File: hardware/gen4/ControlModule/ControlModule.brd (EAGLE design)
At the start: 46.4 x 67 mm, 39 parts, among them IC1 XMEGA16A4A

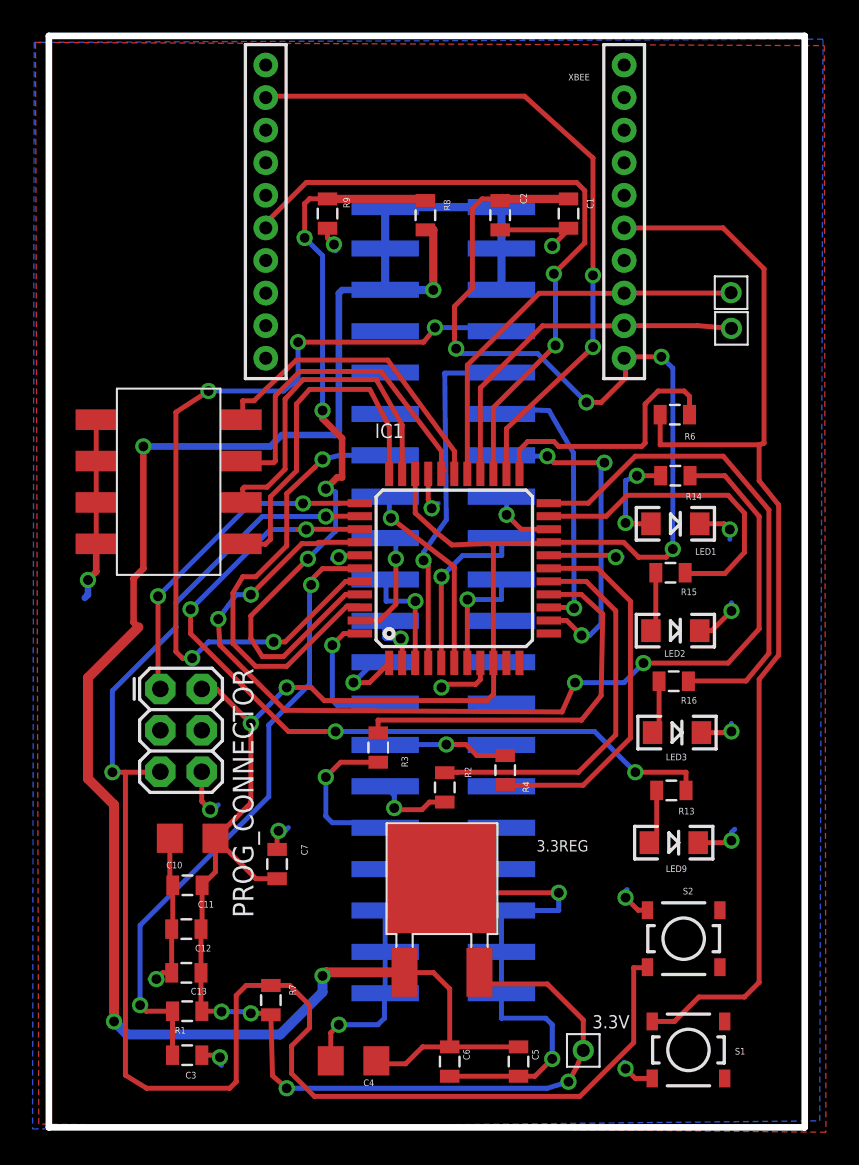
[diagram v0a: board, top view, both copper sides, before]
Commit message: fixed overlaps
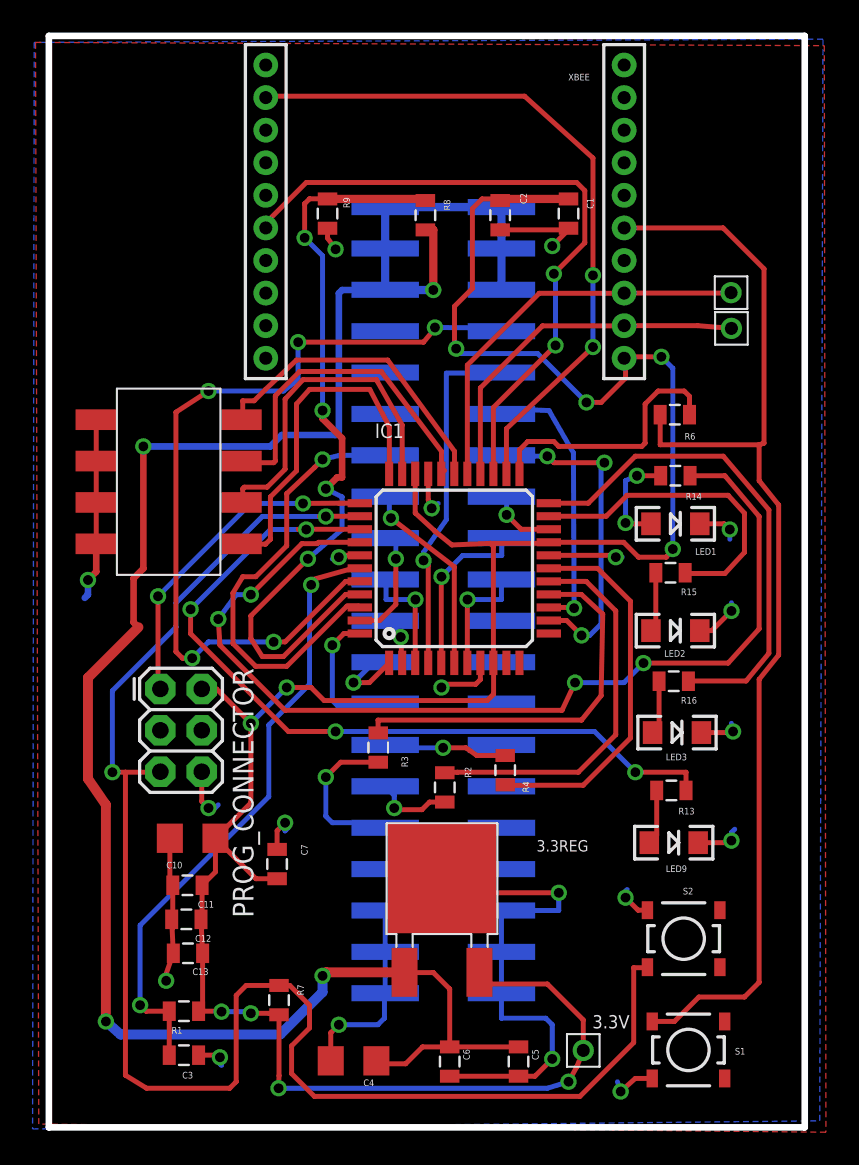
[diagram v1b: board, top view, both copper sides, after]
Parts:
- moved C13 1.20 mm to (32.7, 9.98)
- moved C12 0.60 mm to (32.6, 12.1)
- moved R7 0.50 mm to (38.3, 7.11)
- moved C3 0.20 mm to (32.5, 3.73)
- moved R1 0.20 mm to (32.5, 6.43)
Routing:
- net 3.3V: track 158.7 -> 160.7 mm
- net GND: track 63.8 -> 65.7 mm

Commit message: more gerber files. also all orders went through (technically)
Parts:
- removed PROG_CONNECTOR: FEMALE 2x3, SparkFun-Connectors:2X3
- added JP3: (no value), SparkFun-Connectors:2X5-SHROUDED
- moved C10 6.32 mm to (36.6, 11.8)
- moved C11 6.11 mm to (36.6, 9.46)
- moved R2 1.27 mm to (49.8, 20.2)
- moved C12 0.10 mm to (32.7, 12.1)
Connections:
- net 3.3V: now also JP3.2; no longer PROG_CONNECTOR.2
- net DATA: no longer PROG_CONNECTOR.1
- net GND: now also JP3.10, JP3.4, JP3.6, JP3.8; no longer PROG_CONNECTOR.6
- net MISO: now also JP3.9
- net MOSI: now also JP3.1
- net RESET: now also JP3.5; no longer PROG_CONNECTOR.5
- net SCK: now also JP3.7
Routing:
- net SCK: track 23.1 -> 53.1 mm, vias 0 -> 1
- net GND: track 65.7 -> 94.2 mm, vias 17 -> 19
- net DATA: track 20.5 -> 0.00 mm, vias 2 -> 0
- net MOSI: track 23.9 -> 44.0 mm, vias 0 -> 3
- net MISO: track 24.0 -> 40.3 mm, vias 0 -> 1
- net 3.3V: track 160.7 -> 171.0 mm
- net N$1: track 38.2 -> 40.6 mm
- net N$6: track 4.90 -> 6.17 mm
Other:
- board size 46.4 x 67 mm -> 46.4 x 66.3 mm

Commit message: starting routing
done layout
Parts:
- removed S2: SWITCH-MOMENTARY-2SMD-2, SparkFun-Electromechanical:TACTILE_SWITCH_SMD-2
- added S3: TAC_SWITCHSMD, SparkFun-Retired:TACTILE-SWITCH-SMD
- S1: value SWITCH-MOMENTARY-2SMD-2 -> TAC_SWITCHSMD; device SparkFun-Electromechanical:TACTILE_SWITCH_SMD-2 -> SparkFun-Retired:TACTILE-SWITCH-SMD
- moved 3.3V 50.0 mm to (65.4, 53.3)
- moved C12 45.6 mm to (59.7, 48.9), turned to 180 degrees
- moved C11 43.5 mm to (59.7, 46.4), turned to 180 degrees
- moved R8 41.5 mm to (43.2, 14.0), flipped to the bottom, turned to 0 degrees
- moved C1 41.2 mm to (39.4, 17.8), flipped to the bottom, turned to 0 degrees
- moved R6 40.1 mm to (40.6, 9.53), flipped to the bottom, turned to 0 degrees
- moved R9 39.6 mm to (43.2, 15.9), flipped to the bottom, turned to 180 degrees
- moved C2 37.7 mm to (39.4, 19.7), flipped to the bottom, turned to 180 degrees
- moved JP3 28.4 mm to (61.6, 21.0)
- moved C4 27.3 mm to (39.4, 30.5), flipped to the bottom, turned to 90 degrees
- moved C5 27.0 mm to (39.4, 26.7), flipped to the bottom, turned to 180 degrees
- moved 3.3REG 26.9 mm to (41.9, 40.6), flipped to the bottom
- moved C6 23.4 mm to (39.4, 24.8), flipped to the bottom, turned to 180 degrees
- moved C10 20.2 mm to (44.5, 30.5), flipped to the bottom, turned to 270 degrees
- moved C13 18.5 mm to (43.8, 24.8), flipped to the bottom, turned to 0 degrees
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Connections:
- net GND: now also S1.2, S3.2; no longer S1.1, S2.2
- net RESET: now also S3.4; no longer S2.1
- net XBRST: now also S1.3, S1.4; no longer S1.2
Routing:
- net 3.3V: track 171.0 -> 0.00 mm, vias 10 -> 0
- net 12V: track 122.1 -> 0.00 mm, vias 4 -> 0
- net RESET: track 99.0 -> 0.00 mm, vias 2 -> 0
- net GND: track 94.2 -> 0.00 mm, vias 19 -> 0
- net XBRST: track 70.0 -> 0.00 mm
- net RLED1: track 62.0 -> 0.00 mm, vias 4 -> 0
- net SCK: track 53.1 -> 0.00 mm, vias 1 -> 0
- net BB_IN: track 51.6 -> 0.00 mm, vias 5 -> 0
- net 12VGND: track 50.5 -> 0.00 mm, vias 3 -> 0
- net GLED1: track 49.9 -> 0.00 mm, vias 4 -> 0
- net BATSENSE: track 48.2 -> 0.00 mm, vias 4 -> 0
- net MOSI: track 44.0 -> 0.00 mm, vias 3 -> 0
- net CTS: track 43.3 -> 0.00 mm, vias 2 -> 0
- net RTS: track 40.9 -> 0.00 mm, vias 2 -> 0
- net N$1: track 40.6 -> 0.00 mm, vias 2 -> 0
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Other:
- board size 46.4 x 66.3 mm -> 29.9 x 59.3 mm

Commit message: routing in progress (comms board)
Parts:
- moved R6 6.35 mm to (47.0, 9.53)
- moved C10 5.08 mm to (39.4, 30.5)
- moved C4 5.08 mm to (44.5, 30.5)
- moved C5 5.08 mm to (44.5, 26.7)
- moved C6 5.08 mm to (44.5, 24.8)
- moved C13 4.45 mm to (39.4, 24.8)
- moved C7 4.45 mm to (39.4, 26.7)
- moved R7 4.45 mm to (40.6, 9.53)
- moved C11 2.38 mm to (59.7, 48.7)
- moved C12 1.43 mm to (59.7, 50.3)
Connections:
- net GND: now also S1.1, S3.1
- net RESET: now also S3.3
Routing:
- net 3.3V: track 0.00 -> 45.1 mm, vias 0 -> 1
- net CTS: track 0.00 -> 42.8 mm, vias 0 -> 2
- net TX: track 0.00 -> 34.0 mm
- net GND: track 0.00 -> 33.5 mm
- net RTS: track 0.00 -> 33.3 mm, vias 0 -> 2
- net RX: track 0.00 -> 31.6 mm
- net KICK_REF: track 0.00 -> 31.4 mm, vias 0 -> 1
- net RLED1: track 0.00 -> 30.4 mm, vias 0 -> 2
- net MOSI: track 0.00 -> 29.8 mm, vias 0 -> 3
- net N$5: track 0.00 -> 27.2 mm, vias 0 -> 1
- net GLED2: track 0.00 -> 18.1 mm
- net BID0: track 0.00 -> 15.1 mm
- net BID1: track 0.00 -> 12.8 mm
- net RLED2: track 0.00 -> 12.4 mm
- net BID2: track 0.00 -> 11.0 mm
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
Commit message: routing fun!
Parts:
- moved LED1 32.0 mm to (39.4, 19.1), turned to 90 degrees
- moved R14 27.8 mm to (39.4, 20.3), flipped to the bottom
- moved LED9 25.3 mm to (39.4, 24.8), turned to 90 degrees
- moved R13 21.9 mm to (39.4, 22.9), flipped to the bottom
- moved C2 15.7 mm to (54.0, 14.0), flipped to the top, turned to 270 degrees
- moved R4 14.9 mm to (56.8, 23.7), flipped to the top
- moved R3 13.7 mm to (56.8, 20.5), flipped to the top
- moved R2 13.7 mm to (56.8, 22.1), flipped to the top, turned to 0 degrees
- moved C1 13.3 mm to (52.1, 14.0), flipped to the top, turned to 270 degrees
- moved R9 7.10 mm to (44.5, 22.9)
- moved R8 6.16 mm to (44.5, 20.0)
- moved LED2 4.02 mm to (59.7, 36.2)
- moved R15 4.02 mm to (55.2, 36.2)
- moved LED3 3.86 mm to (59.7, 34.3)
- moved R16 3.86 mm to (55.2, 34.3)
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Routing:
- net BB_OUT: track 0.00 -> 92.5 mm, vias 0 -> 2
- net DISCHARGE: track 0.00 -> 90.3 mm, vias 0 -> 2
- net SS_1: track 0.00 -> 68.8 mm, vias 0 -> 3
- net SS_2: track 0.00 -> 68.4 mm, vias 0 -> 3
- net CHARGE_DONE: track 0.00 -> 68.1 mm, vias 0 -> 2
- net SS_3: track 0.00 -> 68.0 mm, vias 0 -> 3
- net XBRST: track 9.93 -> 76.1 mm, vias 1 -> 3
- net CHARGE: track 0.00 -> 61.2 mm, vias 0 -> 1
- net CHIP_ENABLE: track 0.00 -> 54.5 mm, vias 0 -> 3
- net KICK_ENABLE: track 0.00 -> 54.2 mm, vias 0 -> 2
- net 12V: track 4.97 -> 56.6 mm, vias 0 -> 4
- net BB_IN: track 0.00 -> 46.6 mm, vias 0 -> 2
- net DIVCAP: track 0.00 -> 38.6 mm, vias 0 -> 2
- net DRIB: track 0.00 -> 32.8 mm, vias 0 -> 3
- net KICK_REF: track 31.4 -> 0.00 mm, vias 1 -> 0
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
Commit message: routing comms board done
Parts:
- moved C4 0.16 mm to (44.6, 30.5)
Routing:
- net 3.3V: track 75.1 -> 163.2 mm
- net GND: track 50.6 -> 103.8 mm, vias 6 -> 13
- net RESET: track 24.4 -> 58.6 mm, vias 1 -> 3
- net SS_4: track 0.00 -> 29.6 mm, vias 0 -> 3
- net KICK_REF: track 0.00 -> 26.6 mm, vias 0 -> 1
- net 12VGND: track 32.8 -> 52.7 mm, vias 2 -> 4
- net 12V: track 56.6 -> 70.7 mm
- net DIVCAP: track 38.6 -> 40.5 mm
- net BB_OUT: track 92.5 -> 91.1 mm, vias 2 -> 1
- net SS_2: track 68.4 -> 67.5 mm
- net GLED2: track 14.1 -> 14.8 mm
- net BID2: track 11.6 -> 12.2 mm

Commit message: almost done
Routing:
- net SS_4: track 29.6 -> 30.8 mm
- net N$6: track 11.9 -> 12.9 mm
- net CHARGE_DONE: track 68.1 -> 68.5 mm, vias 2 -> 1
- net BB_IN: track 46.6 -> 46.4 mm, vias 2 -> 1
- net 12V: vias 4 -> 3
- net KICK_ENABLE: vias 2 -> 1
- net DIVCAP: vias 2 -> 1
- net DISCHARGE: vias 2 -> 1

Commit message: comms board done I think
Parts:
- removed JP3: (no value), SparkFun-Connectors:2X5-SHROUDED
- added JP2: (no value), pinhead:2X03
- moved C5 0.48 mm to (44.5, 26.2)
- moved R3 0.24 mm to (56.8, 20.2)
- moved R6 0.16 mm to (47.0, 9.37)
- moved R9 0.16 mm to (44.5, 22.7)
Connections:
- net 3.3V: now also JP2.2; no longer JP3.2
- net DATA: now also JP2.1
- net GND: now also JP2.6; no longer JP3.10, JP3.4, JP3.6, JP3.8
- net MISO: no longer JP3.9
- net MOSI: no longer JP3.1
- net RESET: now also JP2.5; no longer JP3.5
- net SCK: no longer JP3.7
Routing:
- net SS_4: track 30.8 -> 38.4 mm
- net GND: track 104.1 -> 111.1 mm
- net MOSI: track 8.78 -> 1.88 mm
- net N$7: track 13.1 -> 16.3 mm, vias 1 -> 3
- net N$8: track 12.7 -> 15.0 mm
- net MISO: track 10.0 -> 8.04 mm
- net BATSENSE: track 7.35 -> 5.66 mm
- net SCK: track 20.1 -> 18.4 mm
- net 12VGND: track 52.7 -> 54.2 mm
- net N$6: track 12.9 -> 14.0 mm
- net 12V: track 70.7 -> 71.4 mm
- net DIVCAP: track 40.5 -> 39.8 mm
- net N$2: track 2.57 -> 3.21 mm
